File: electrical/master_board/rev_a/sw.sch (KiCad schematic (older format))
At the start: 27 parts, among them CN108 BRIDGE_SW_OUTER;M1x8, Q10 2N7000;SOT23, Q11 2N7000;SOT23, Q7 2N7000;SOT23, Q8 2N7000;SOT23, Q9 2N7000;SOT23

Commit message: Got NE PCB done.
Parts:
- R21, R22, R23, R24, R25, R26, R27, R28, R29, R30, R31, R32, R33, R34, R35: value 330;1608 -> 330Ω;1608
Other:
- note added: "Notes:\n1. GRNRA = Green Right Angle Green\n2. Nominal Part:\n Mfg Part #: TLPG5600\n Digi-Key part #: TLPG5600-ND\n Forward Voltage Drop: 2.4V\n Absolute max. current: 200mA\n Target maximum current: I=60mA\n Resistor: R = (9V - 2.4V) / 75mA = 6.6V / .060A = 110Ω\n Watts: W = I**2*R = (.060 * .060) * 110 = .396W ~~=.4W\n Use 3 x 330Ω in parallel to get 110Ω\n Watts per resistor: Wr = .4W / 3 = .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"
- note removed: "Note: GRNRA = Green Right Angle 0.254mm (approx.) lead spacing"
- note removed: "Note: LED's are labeled from 1 to 16 in a clockwise\ndirection starting in the NW quadrant near the X axis."
- note removed: "Right Angle Green LED\nMfg Part #: TLPG5600\nDigi-Key part #: TLPG5600-ND\nForward Voltage Drop: 2.4V\nAbsolute max. current: 200mA\nTarget current: I=60mA\nR = (9V - 2.4V) / 75mA = 6.6V / .060A = 110Ohm\nW=I**2*R = (.060 * .060) * 110=.495W = .396W =.4W\nUse 3 330Ohm resistors in parallel to get 110Ohm\n1/8 Watt or larger should work.\n\n.\n"
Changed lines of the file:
@@
 P 7850 3500
 F 0 "R34" V 7750 3400 50  0000 L CNN
-F 1 "330;1608" V 7950 3300 50  0000 L CNN
+F 1 "330Ω;1608" V 7950 3300 50  0000 L CNN
 F 2 "Resistor_SMD:R_0603_1608Metric" V 7890 3490 50  0001 C CNN
 F 3 "~" H 7850 3500 50  0001 C CNN
@@
 $EndComp
 Text Notes 2800 6450 0    50   ~ 0
-Right Angle Green LED\nMfg Part #: TLPG5600\nDigi-Key part #: TLPG5600-ND\nForward Voltage Drop: 2.4V\nAbsolute max. current: 200mA\nTarget current: I=60mA\nR = (9V - 2.4V) / 75mA = 6.6V / .060A = 110Ohm\nW=I**2*R = (.060 * .060) * 110=.495W = .396W =.4W\nUse 3 330Ohm resistors in parallel to get 110Ohm\n1/8 Watt or larger should work.\n\n.\n
+Notes:\n1. GRNRA = Green Right Angle Green\n2. Nominal Part:\n     Mfg Part #: TLPG5600\n     Digi-Key part #: TLPG5600-ND\n     Forward Voltage Drop: 2.4V\n     Absolute max. current: 200mA\n     Target maximum current: I=60mA\n     Resistor: R = (9V - 2.4V) / 75mA = 6.6V / .060A = 110Ω\n     Watts: W = I**2*R = (.060 * .060) * 110 = .396W ~~=.4W\n     Use 3 x 330Ω in parallel to get 110Ω\n     Watts per resistor: Wr = .4W / 3 = .133W ~~= .125W\n     1/8W or larger should work.\n3. LED's and transistors are labeled from 1 to 16 in a clockwise\n     direction starting in the NW quadrant near the X axis.  The\n     resesitors are labeld Ra, Rb, and Rc, where a=3*n-2, b=3*n-1,\n     and c=3*n, where n is the LED number.
 Wire Wire Line
 	8100 4400 8100 4300
@@
 P 7850 3200
 F 0 "R33" V 7750 3100 50  0000 L CNN
-F 1 "330;1608" V 7950 3000 50  0000 L CNN
+F 1 "330Ω;1608" V 7950 3000 50  0000 L CNN
 F 2 "Resistor_SMD:R_0603_1608Metric" V 7890 3190 50  0001 C CNN
 F 3 "~" H 7850 3200 50  0001 C CNN
@@
 P 7850 3800
 F 0 "R35" V 7750 3700 50  0000 L CNN
-F 1 "330;1608" V 7950 3600 50  0000 L CNN
+F 1 "330Ω;1608" V 7950 3600 50  0000 L CNN
 F 2 "Resistor_SMD:R_0603_1608Metric" V 7890 3790 50  0001 C CNN
 F 3 "~" H 7850 3800 50  0001 C CNN
@@
 P 6950 3500
 F 0 "R31" V 6850 3400 50  0000 L CNN
-F 1 "330;1608" V 7050 3300 50  0000 L CNN
+F 1 "330Ω;1608" V 7050 3300 50  0000 L CNN
 F 2 "Resistor_SMD:R_0603_1608Metric" V 6990 3490 50  0001 C CNN
 F 3 "~" H 6950 3500 50  0001 C CNN
@@
 P 6950 3200
 F 0 "R30" V 6850 3100 50  0000 L CNN
-F 1 "330;1608" V 7050 3000 50  0000 L CNN
+F 1 "330Ω;1608" V 7050 3000 50  0000 L CNN
 F 2 "Resistor_SMD:R_0603_1608Metric" V 6990 3190 50  0001 C CNN
 F 3 "~" H 6950 3200 50  0001 C CNN
@@
 P 6950 3800
 F 0 "R32" V 6850 3700 50  0000 L CNN
-F 1 "330;1608" V 7050 3600 50  0000 L CNN
+F 1 "330Ω;1608" V 7050 3600 50  0000 L CNN
 F 2 "Resistor_SMD:R_0603_1608Metric" V 6990 3790 50  0001 C CNN
 F 3 "~" H 6950 3800 50  0001 C CNN
@@
 P 5150 3500
 F 0 "R25" V 5050 3400 50  0000 L CNN
-F 1 "330;1608" V 5250 3300 50  0000 L CNN
+F 1 "330Ω;1608" V 5250 3300 50  0000 L CNN
 F 2 "Resistor_SMD:R_0603_1608Metric" V 5190 3490 50  0001 C CNN
 F 3 "~" H 5150 3500 50  0001 C CNN
@@
 P 5150 3200
 F 0 "R24" V 5050 3100 50  0000 L CNN
-F 1 "330;1608" V 5250 3000 50  0000 L CNN
+F 1 "330Ω;1608" V 5250 3000 50  0000 L CNN
 F 2 "Resistor_SMD:R_0603_1608Metric" V 5190 3190 50  0001 C CNN
 F 3 "~" H 5150 3200 50  0001 C CNN
@@
 P 5150 3800
 F 0 "R26" V 5050 3700 50  0000 L CNN
-F 1 "330;1608" V 5250 3600 50  0000 L CNN
+F 1 "330Ω;1608" V 5250 3600 50  0000 L CNN
 F 2 "Resistor_SMD:R_0603_1608Metric" V 5190 3790 50  0001 C CNN
 F 3 "~" H 5150 3800 50  0001 C CNN
@@
 P 4250 3500
 F 0 "R22" V 4150 3400 50  0000 L CNN
-F 1 "330;1608" V 4350 3300 50  0000 L CNN
+F 1 "330Ω;1608" V 4350 3300 50  0000 L CNN
 F 2 "Resistor_SMD:R_0603_1608Metric" V 4290 3490 50  0001 C CNN
 F 3 "~" H 4250 3500 50  0001 C CNN
@@
 P 4250 3200
 F 0 "R21" V 4150 3100 50  0000 L CNN
-F 1 "330;1608" V 4350 3000 50  0000 L CNN
+F 1 "330Ω;1608" V 4350 3000 50  0000 L CNN
 F 2 "Resistor_SMD:R_0603_1608Metric" V 4290 3190 50  0001 C CNN
 F 3 "~" H 4250 3200 50  0001 C CNN
@@
 P 4250 3800
 F 0 "R23" V 4150 3700 50  0000 L CNN
-F 1 "330;1608" V 4350 3600 50  0000 L CNN
+F 1 "330Ω;1608" V 4350 3600 50  0000 L CNN
 F 2 "Resistor_SMD:R_0603_1608Metric" V 4290 3790 50  0001 C CNN
 F 3 "~" H 4250 3800 50  0001 C CNN
@@
 P 6050 3800
 F 0 "R29" V 5950 3700 50  0000 L CNN
-F 1 "330;1608" V 6150 3600 50  0000 L CNN
+F 1 "330Ω;1608" V 6150 3600 50  0000 L CNN
 F 2 "Resistor_SMD:R_0603_1608Metric" V 6090 3790 50  0001 C CNN
 F 3 "~" H 6050 3800 50  0001 C CNN
@@
 P 6050 3200
 F 0 "R27" V 5950 3100 50  0000 L CNN
-F 1 "330;1608" V 6150 3000 50  0000 L CNN
+F 1 "330Ω;1608" V 6150 3000 50  0000 L CNN
 F 2 "Resistor_SMD:R_0603_1608Metric" V 6090 3190 50  0001 C CNN
 F 3 "~" H 6050 3200 50  0001 C CNN
@@
 P 6050 3500
 F 0 "R28" V 5950 3400 50  0000 L CNN
-F 1 "330;1608" V 6150 3300 50  0000 L CNN
+F 1 "330Ω;1608" V 6150 3300 50  0000 L CNN
 F 2 "Resistor_SMD:R_0603_1608Metric" V 6090 3490 50  0001 C CNN
 F 3 "~" H 6050 3500 50  0001 C CNN
@@
 Text Label 3650 2900 0    50   ~ 0
 9V
-Text Notes 2800 6850 0    50   ~ 0
-Note: GRNRA = Green Right Angle 0.254mm (approx.) lead spacing
-Text Notes 2800 6600 0    50   ~ 0
-Note: LED's are labeled from 1 to 16 in a clockwise\ndirection starting in the NW quadrant near the X axis.
 Text Notes 2150 4250 0    50   ~ 0
 Note: Mounting Hole for above\narm expansion plates.

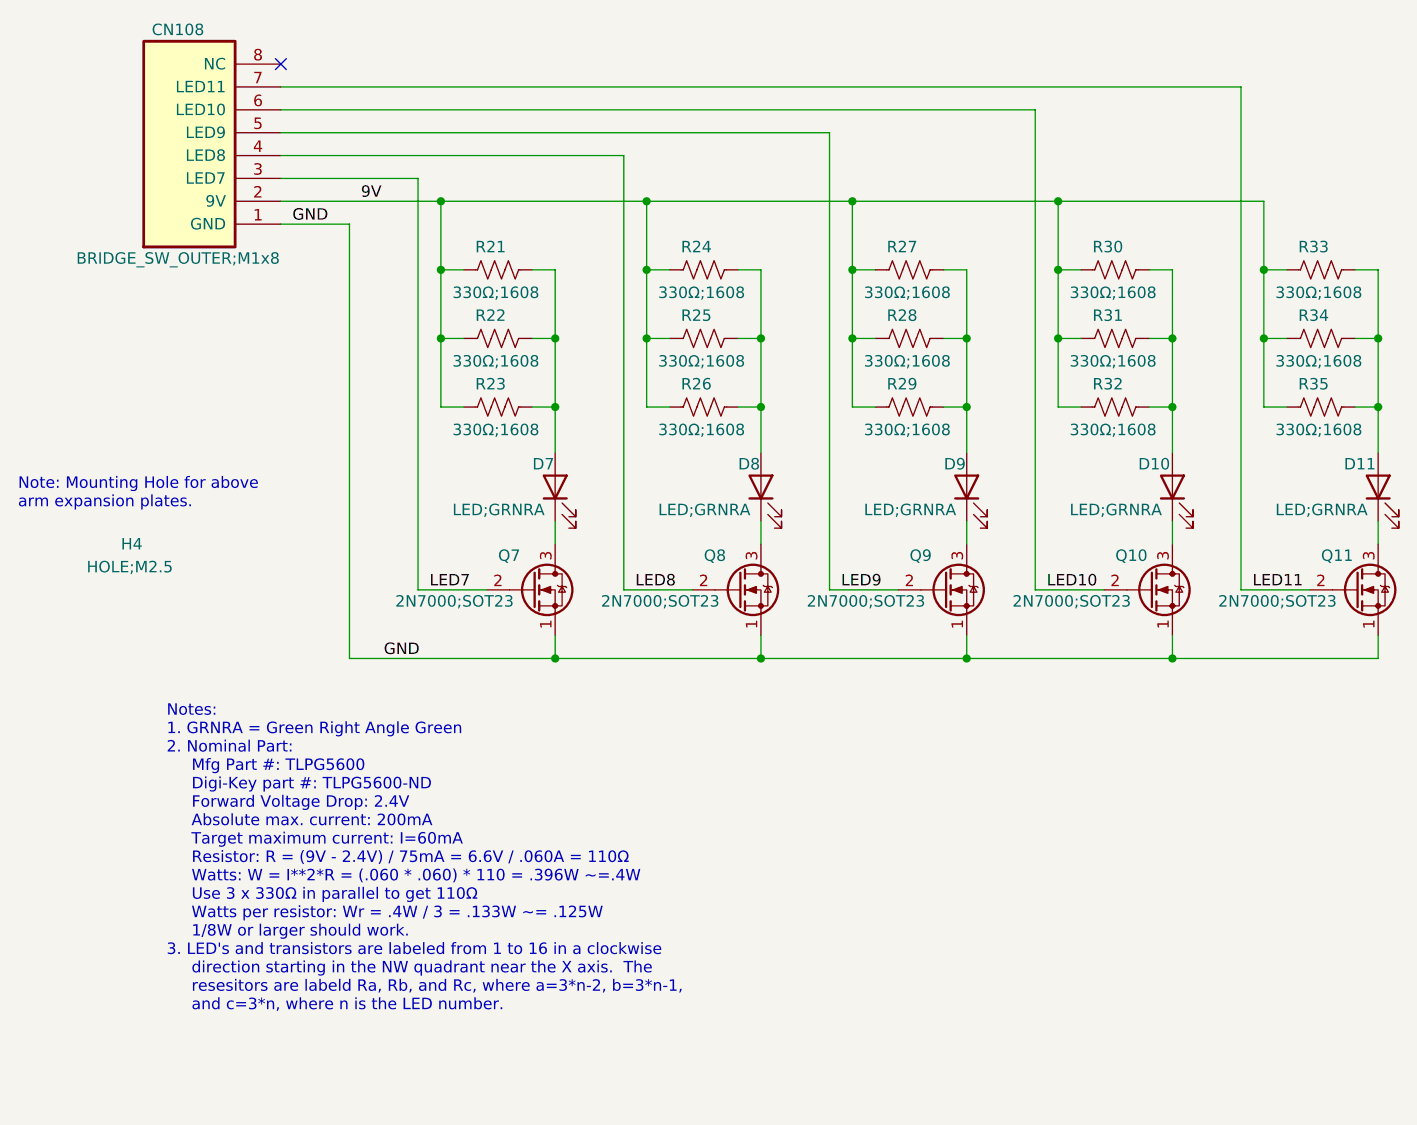
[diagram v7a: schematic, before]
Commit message: Linked the NE/NW/SE/SW sheets to master_board.
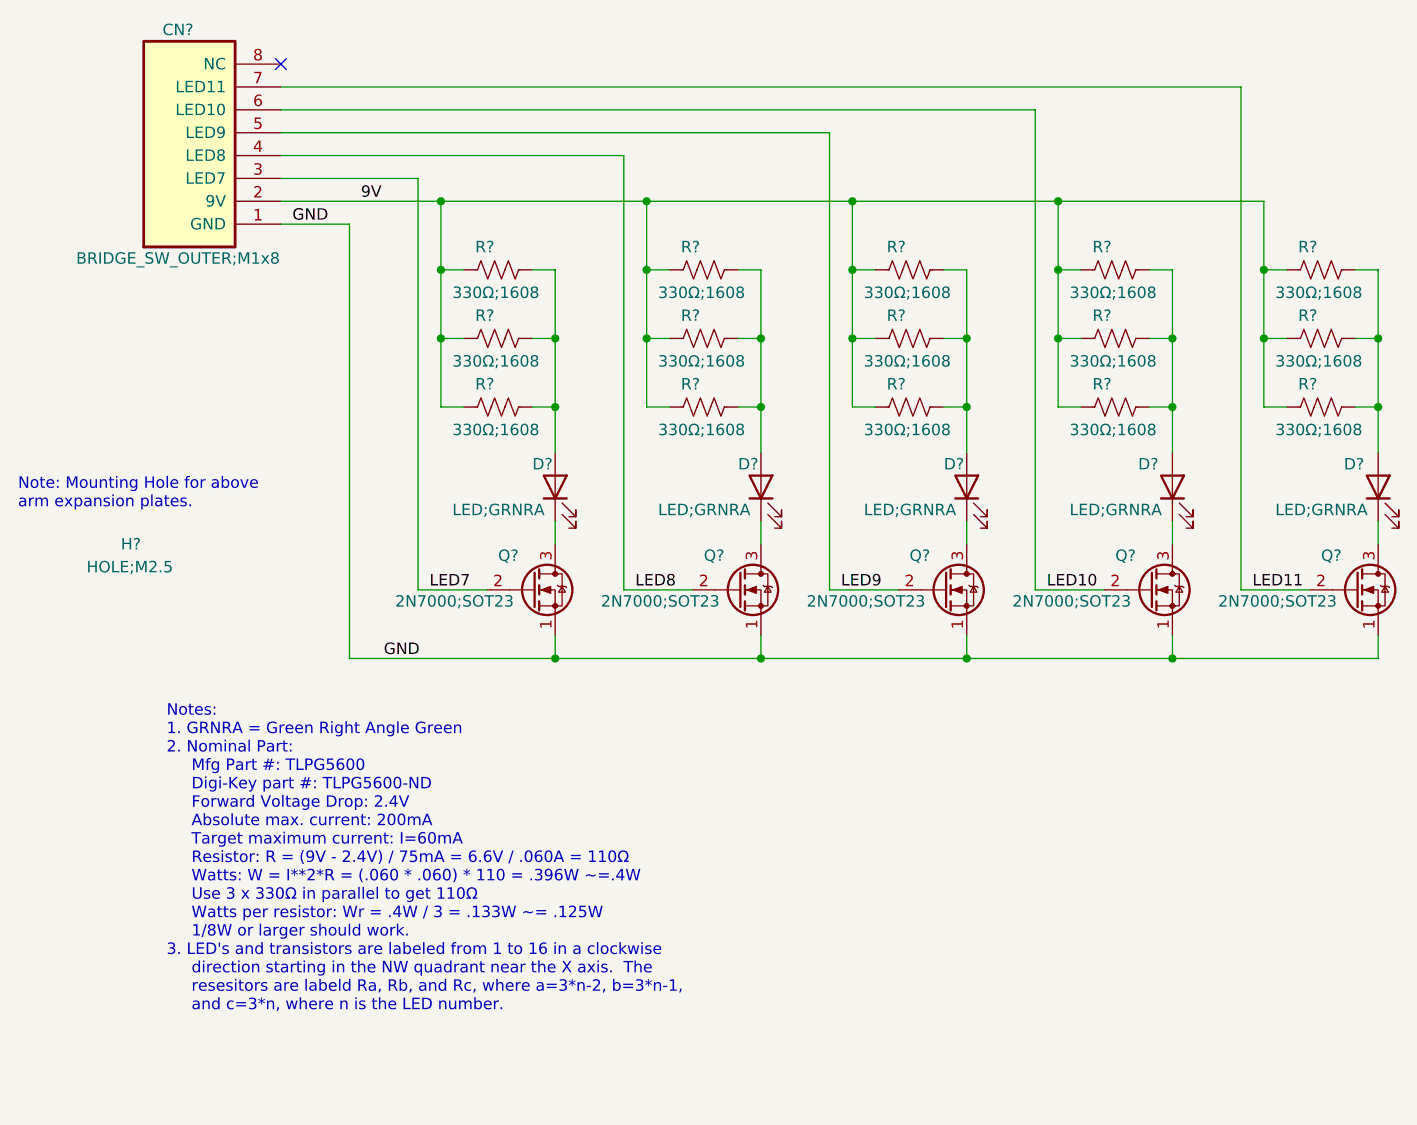
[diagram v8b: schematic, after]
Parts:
- renumbered CN108 to CN?, D7 to D?, D8 to D?, D9 to D?, D10 to D?, D11 to D?, H4 to H?, Q11 to Q?, Q10 to Q?, Q9 to Q?, Q8 to Q?, Q7 to Q?, R34 to R?, R33 to R?, R35 to R?, R31 to R?, R30 to R?, R32 to R?, R28 to R?, R27 to R?, R29 to R?, R25 to R?, R24 to R?, R26 to R?, R22 to R?, R21 to R?, R23 to R?
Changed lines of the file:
@@
 $Descr A 11000 8500
 encoding utf-8
-Sheet 1 1
+Sheet 11 12
 Title "HR2 SW PCB"
 Date "2020-06-13"
@@
 $EndDescr
 $Comp
-L HR2:HOLE;M2.5 H4
+L HR2:HOLE;M2.5 H?
 U 1 1 5F2F7A6B
 P 2650 4450
-F 0 "H4" H 2600 4500 50  0000 L CNN
+F 0 "H?" H 2600 4500 50  0000 L CNN
 F 1 "HOLE;M2.5" H 2450 4400 50  0000 L CNN
 F 2 "MountingHole:MountingHole_2.7mm_M2.5" H 2850 4500 60  0001 L CNN
@@
 $EndComp
 $Comp
-L Device:LED D8
+L Device:LED D?
 U 1 1 5F30CB7A
 P 5400 4150
-F 0 "D8" V 5500 4250 50  0000 R CNN
+F 0 "D?" V 5500 4250 50  0000 R CNN
 F 1 "LED;GRNRA" V 5300 4600 50  0000 R CNN
 F 2 "HR2:LED_GRNRA" H 5400 4150 50  0001 C CNN
@@
 $EndComp
 $Comp
-L Device:LED D10
+L Device:LED D?
 U 1 1 5F30CF92
 P 7200 4150
-F 0 "D10" V 7300 4300 50  0000 R CNN
+F 0 "D?" V 7300 4300 50  0000 R CNN
 F 1 "LED;GRNRA" V 7100 4600 50  0000 R CNN
 F 2 "HR2:LED_GRNRA" H 7200 4150 50  0001 C CNN
@@
 $EndComp
 $Comp
-L Device:LED D11
+L Device:LED D?
 U 1 1 5F30EB24
 P 8100 4150
-F 0 "D11" V 8200 4300 50  0000 R CNN
+F 0 "D?" V 8200 4300 50  0000 R CNN
 F 1 "LED;GRNRA" V 8000 4600 50  0000 R CNN
 F 2 "HR2:LED_GRNRA" H 8100 4150 50  0001 C CNN
@@
 $EndComp
 $Comp
-L HR2:BRIDGE_SW_OUTER;M1x8 CN108
+L HR2:BRIDGE_SW_OUTER;M1x8 CN?
 U 1 1 5F387C15
 P 2500 3000
-F 0 "CN108" H 2850 2150 50  0000 C CNN
+F 0 "CN?" H 2850 2150 50  0000 C CNN
 F 1 "BRIDGE_SW_OUTER;M1x8" H 2850 3150 50  0000 C CNN
 F 2 "HR2:BRIDGE_SW_OUTER_M1x8" H 2700 3050 60  0001 L CNN
@@
 GND
 $Comp
-L Transistor_FET:2N7000 Q11
+L Transistor_FET:2N7000 Q?
 U 1 1 5F39F103
 P 8000 4600
-F 0 "Q11" H 7850 4750 50  0000 L CNN
+F 0 "Q?" H 7850 4750 50  0000 L CNN
 F 1 "2N7000;SOT23" H 7400 4550 50  0000 L CNN
 F 2 "Package_TO_SOT_SMD:SOT-23" H 8200 4525 50  0001 L CIN
@@
 $EndComp
 $Comp
-L Device:R_US R34
+L Device:R_US R?
 U 1 1 5F3A3A4B
 P 7850 3500
-F 0 "R34" V 7750 3400 50  0000 L CNN
+F 0 "R?" V 7750 3400 50  0000 L CNN
 F 1 "330Ω;1608" V 7950 3300 50  0000 L CNN
 F 2 "Resistor_SMD:R_0603_1608Metric" V 7890 3490 50  0001 C CNN
@@
 	8100 4400 8100 4300
 $Comp
-L Device:R_US R33
+L Device:R_US R?
 U 1 1 5F3A820E
 P 7850 3200
-F 0 "R33" V 7750 3100 50  0000 L CNN
+F 0 "R?" V 7750 3100 50  0000 L CNN
 F 1 "330Ω;1608" V 7950 3000 50  0000 L CNN
 F 2 "Resistor_SMD:R_0603_1608Metric" V 7890 3190 50  0001 C CNN
@@
 $EndComp
 $Comp
-L Device:R_US R35
+L Device:R_US R?
 U 1 1 5F3A878F
 P 7850 3800
-F 0 "R35" V 7750 3700 50  0000 L CNN
+F 0 "R?" V 7750 3700 50  0000 L CNN
 F 1 "330Ω;1608" V 7950 3600 50  0000 L CNN
 F 2 "Resistor_SMD:R_0603_1608Metric" V 7890 3790 50  0001 C CNN
@@
 	7200 4900 7200 4800
 $Comp
-L Transistor_FET:2N7000 Q10
+L Transistor_FET:2N7000 Q?
 U 1 1 5F3B5AC4
 P 7100 4600
-F 0 "Q10" H 6950 4750 50  0000 L CNN
+F 0 "Q?" H 6950 4750 50  0000 L CNN
 F 1 "2N7000;SOT23" H 6500 4550 50  0000 L CNN
 F 2 "Package_TO_SOT_SMD:SOT-23" H 7300 4525 50  0001 L CIN
@@
 $EndComp
 $Comp
-L Device:R_US R31
+L Device:R_US R?
 U 1 1 5F3B5ACE
 P 6950 3500
-F 0 "R31" V 6850 3400 50  0000 L CNN
+F 0 "R?" V 6850 3400 50  0000 L CNN
 F 1 "330Ω;1608" V 7050 3300 50  0000 L CNN
 F 2 "Resistor_SMD:R_0603_1608Metric" V 6990 3490 50  0001 C CNN
@@
 	7200 4400 7200 4300
 $Comp
-L Device:R_US R30
+L Device:R_US R?
 U 1 1 5F3B5AD9
 P 6950 3200
-F 0 "R30" V 6850 3100 50  0000 L CNN
+F 0 "R?" V 6850 3100 50  0000 L CNN
 F 1 "330Ω;1608" V 7050 3000 50  0000 L CNN
 F 2 "Resistor_SMD:R_0603_1608Metric" V 6990 3190 50  0001 C CNN
@@
 $EndComp
 $Comp
-L Device:R_US R32
+L Device:R_US R?
 U 1 1 5F3B5AE3
 P 6950 3800
-F 0 "R32" V 6850 3700 50  0000 L CNN
+F 0 "R?" V 6850 3700 50  0000 L CNN
 F 1 "330Ω;1608" V 7050 3600 50  0000 L CNN
 F 2 "Resistor_SMD:R_0603_1608Metric" V 6990 3790 50  0001 C CNN
@@
 	5400 4900 5400 4800
 $Comp
-L Transistor_FET:2N7000 Q8
+L Transistor_FET:2N7000 Q?
 U 1 1 5F3B8D4A
 P 5300 4600
-F 0 "Q8" H 5150 4750 50  0000 L CNN
+F 0 "Q?" H 5150 4750 50  0000 L CNN
 F 1 "2N7000;SOT23" H 4700 4550 50  0000 L CNN
 F 2 "Package_TO_SOT_SMD:SOT-23" H 5500 4525 50  0001 L CIN
@@
 $EndComp
 $Comp
-L Device:R_US R25
+L Device:R_US R?
 U 1 1 5F3B8D54
 P 5150 3500
-F 0 "R25" V 5050 3400 50  0000 L CNN
+F 0 "R?" V 5050 3400 50  0000 L CNN
 F 1 "330Ω;1608" V 5250 3300 50  0000 L CNN
 F 2 "Resistor_SMD:R_0603_1608Metric" V 5190 3490 50  0001 C CNN
@@
 	5400 4400 5400 4300
 $Comp
-L Device:R_US R24
+L Device:R_US R?
 U 1 1 5F3B8D5F
 P 5150 3200
-F 0 "R24" V 5050 3100 50  0000 L CNN
+F 0 "R?" V 5050 3100 50  0000 L CNN
 F 1 "330Ω;1608" V 5250 3000 50  0000 L CNN
 F 2 "Resistor_SMD:R_0603_1608Metric" V 5190 3190 50  0001 C CNN
@@
 $EndComp
 $Comp
-L Device:R_US R26
+L Device:R_US R?
 U 1 1 5F3B8D69
 P 5150 3800
-F 0 "R26" V 5050 3700 50  0000 L CNN
+F 0 "R?" V 5050 3700 50  0000 L CNN
 F 1 "330Ω;1608" V 5250 3600 50  0000 L CNN
 F 2 "Resistor_SMD:R_0603_1608Metric" V 5190 3790 50  0001 C CNN
@@
 	4500 4900 4500 4800
 $Comp
-L Transistor_FET:2N7000 Q7
+L Transistor_FET:2N7000 Q?
 U 1 1 5F3BEA19
 P 4400 4600
-F 0 "Q7" H 4250 4750 50  0000 L CNN
+F 0 "Q?" H 4250 4750 50  0000 L CNN
 F 1 "2N7000;SOT23" H 3800 4550 50  0000 L CNN
 F 2 "Package_TO_SOT_SMD:SOT-23" H 4600 4525 50  0001 L CIN
@@
 $EndComp
 $Comp
-L Device:R_US R22
+L Device:R_US R?
 U 1 1 5F3BEA23
 P 4250 3500
-F 0 "R22" V 4150 3400 50  0000 L CNN
+F 0 "R?" V 4150 3400 50  0000 L CNN
 F 1 "330Ω;1608" V 4350 3300 50  0000 L CNN
 F 2 "Resistor_SMD:R_0603_1608Metric" V 4290 3490 50  0001 C CNN
@@
 $EndComp
 $Comp
-L Device:R_US R21
+L Device:R_US R?
 U 1 1 5F3BEA2E
 P 4250 3200
-F 0 "R21" V 4150 3100 50  0000 L CNN
+F 0 "R?" V 4150 3100 50  0000 L CNN
 F 1 "330Ω;1608" V 4350 3000 50  0000 L CNN
 F 2 "Resistor_SMD:R_0603_1608Metric" V 4290 3190 50  0001 C CNN
@@
 $EndComp
 $Comp
-L Device:R_US R23
+L Device:R_US R?
 U 1 1 5F3BEA38
 P 4250 3800
-F 0 "R23" V 4150 3700 50  0000 L CNN
+F 0 "R?" V 4150 3700 50  0000 L CNN
 F 1 "330Ω;1608" V 4350 3600 50  0000 L CNN
 F 2 "Resistor_SMD:R_0603_1608Metric" V 4290 3790 50  0001 C CNN
@@
 	4500 4000 4500 3800
 $Comp
-L Device:LED D7
+L Device:LED D?
 U 1 1 5F30BFB1
 P 4500 4150
-F 0 "D7" V 4600 4250 50  0000 R CNN
+F 0 "D?" V 4600 4250 50  0000 R CNN
 F 1 "LED;GRNRA" V 4400 4600 50  0000 R CNN
 F 2 "HR2:LED_GRNRA" H 4500 4150 50  0001 C CNN
@@
 	6200 3800 6300 3800
 $Comp
-L Device:R_US R29
+L Device:R_US R?
 U 1 1 5F3B8D25
 P 6050 3800
-F 0 "R29" V 5950 3700 50  0000 L CNN
+F 0 "R?" V 5950 3700 50  0000 L CNN
 F 1 "330Ω;1608" V 6150 3600 50  0000 L CNN
 F 2 "Resistor_SMD:R_0603_1608Metric" V 6090 3790 50  0001 C CNN
@@
 $EndComp
 $Comp
-L Device:R_US R27
+L Device:R_US R?
 U 1 1 5F3B8D1B
 P 6050 3200
-F 0 "R27" V 5950 3100 50  0000 L CNN
+F 0 "R?" V 5950 3100 50  0000 L CNN
 F 1 "330Ω;1608" V 6150 3000 50  0000 L CNN
 F 2 "Resistor_SMD:R_0603_1608Metric" V 6090 3190 50  0001 C CNN
@@
 	6300 4400 6300 4300
 $Comp
-L Device:R_US R28
+L Device:R_US R?
 U 1 1 5F3B8D10
 P 6050 3500
-F 0 "R28" V 5950 3400 50  0000 L CNN
+F 0 "R?" V 5950 3400 50  0000 L CNN
 F 1 "330Ω;1608" V 6150 3300 50  0000 L CNN
 F 2 "Resistor_SMD:R_0603_1608Metric" V 6090 3490 50  0001 C CNN
@@
 $EndComp
 $Comp
-L Transistor_FET:2N7000 Q9
+L Transistor_FET:2N7000 Q?
 U 1 1 5F3B8D06
 P 6200 4600
-F 0 "Q9" H 6050 4750 50  0000 L CNN
+F 0 "Q?" H 6050 4750 50  0000 L CNN
 F 1 "2N7000;SOT23" H 5600 4550 50  0000 L CNN
 F 2 "Package_TO_SOT_SMD:SOT-23" H 6400 4525 50  0001 L CIN
@@
 	6300 4900 6300 4800
 $Comp
-L Device:LED D9
+L Device:LED D?
 U 1 1 5F30CF88
 P 6300 4150
-F 0 "D9" V 6400 4250 50  0000 R CNN
+F 0 "D?" V 6400 4250 50  0000 R CNN
 F 1 "LED;GRNRA" V 6200 4600 50  0000 R CNN
 F 2 "HR2:LED_GRNRA" H 6300 4150 50  0001 C CNN
